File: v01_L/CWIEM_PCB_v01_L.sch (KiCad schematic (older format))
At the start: 10 parts, among them SW1 SW_PUSH, SW2 SW_PUSH, U1 BC127

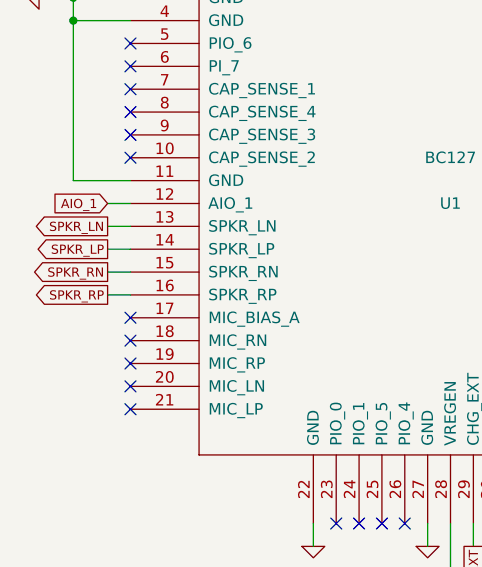
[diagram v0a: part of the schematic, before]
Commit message: Update includes removing right side of audio circuit
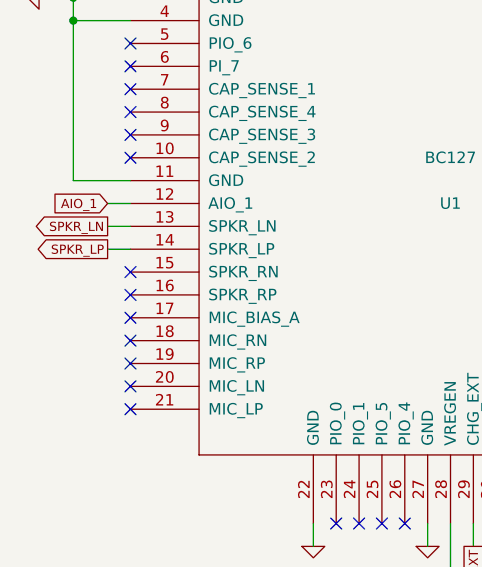
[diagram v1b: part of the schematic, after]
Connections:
- net SPKR_RN: no longer names the net of U1.15 (SPKR_RN)
- net SPKR_RP: no longer names the net of U1.16 (SPKR_RP)
- no-connect marks 25 -> 27
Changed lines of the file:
@@
 Sheet 1 4
 Title "BC127 circuit"
-Date "7 dec 2014"
+Date "16 jan 2015"
 Rev "0"
 Comp ""
@@
 Text GLabel 4000 3700 0    40   Output ~ 0
 SPKR_LP
-Text GLabel 4000 3800 0    40   Output ~ 0
-SPKR_RN
-Text GLabel 4000 3900 0    40   Output ~ 0
-SPKR_RP
 $Sheet
 S 11900 1700 1650 1400
@@
 	4100 3700 4000 3700
 Wire Wire Line
-	4000 3800 4100 3800
-Wire Wire Line
-	4100 3900 4000 3900
-Wire Wire Line
 	7050 3700 6900 3700
 Wire Wire Line
@@
 	3850 3400 4100 3400
 Connection ~ 3850 2700
+NoConn ~ 4100 3800
+NoConn ~ 4100 3900
 $EndSCHEMATC
